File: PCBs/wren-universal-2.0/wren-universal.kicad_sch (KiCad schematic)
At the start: 121 parts, among them J1 TRRS_Jack, J2 Nice!Nano Compatibility, SW0 Reset, U1 Elite-C, U2 EGG PRO MICRO

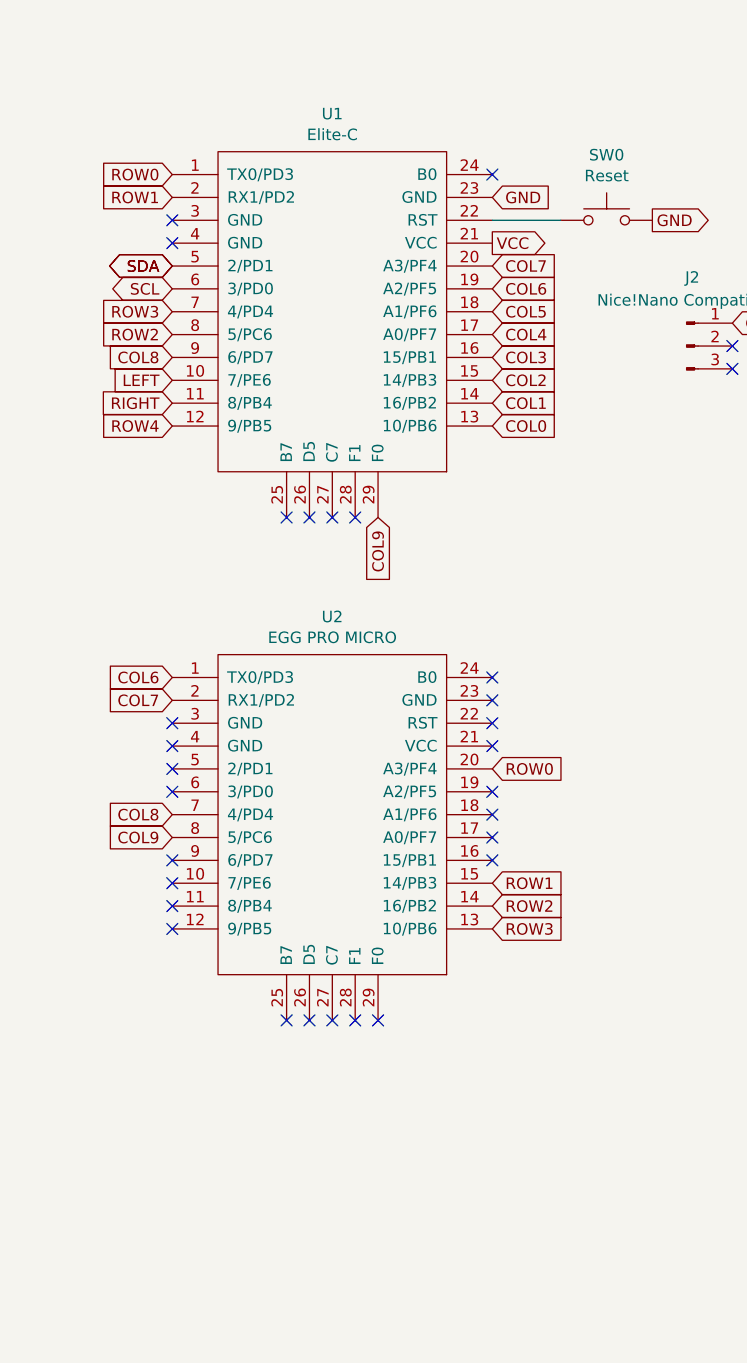
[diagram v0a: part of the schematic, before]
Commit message: Add battery header, update readme
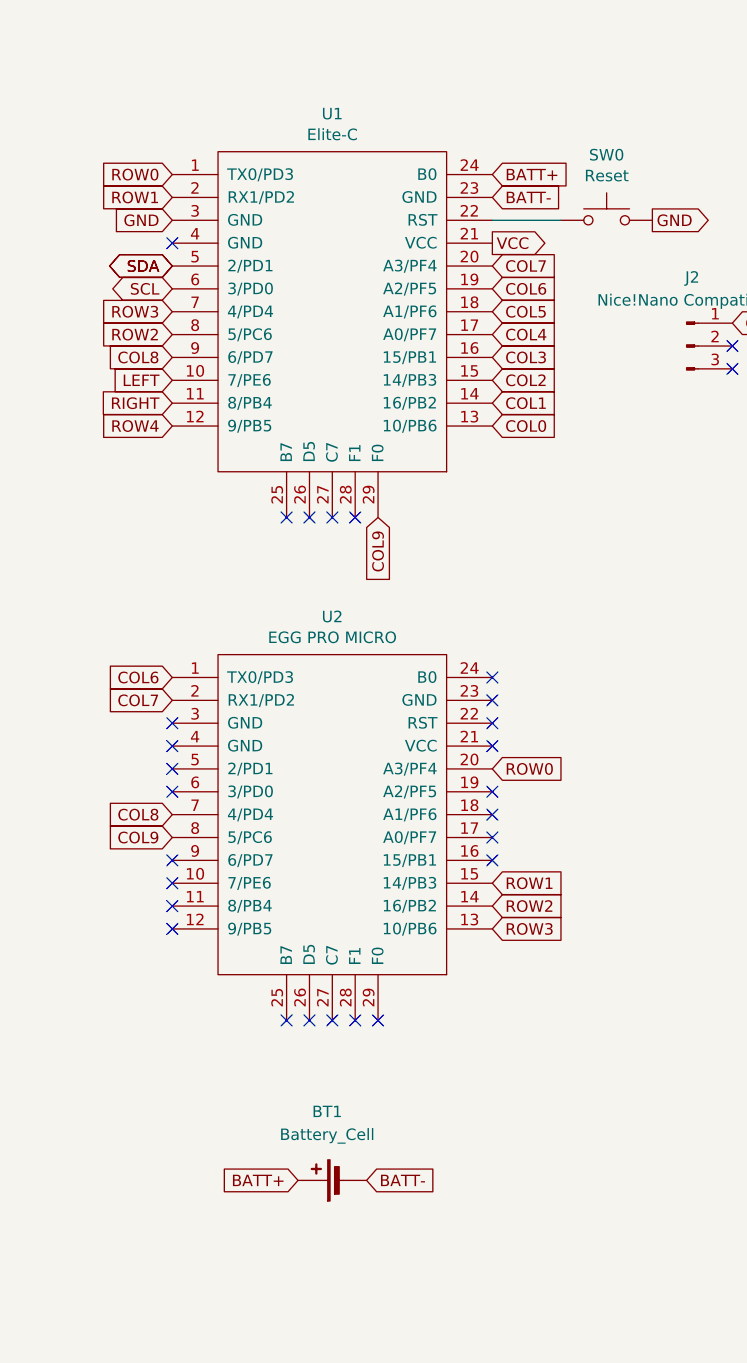
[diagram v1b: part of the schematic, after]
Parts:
- added BT1: Battery_Cell, Connector_PinHeader_2.00mm:PinHeader_1x02_P2.00mm_Vertical, symbol Device:Battery_Cell
- J2: footprint Connector_PinHeader_1.00mm:PinHeader_1x03_P1.00mm_Horizontal -> Connector_PinHeader_2.54mm:PinHeader_1x03_P2.54mm_Vertical
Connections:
- net GND: now also U1.3 (GND); no longer U1.23 (GND)
- net BATT+: now reaches U1.24 (B0)
- net BATT+: now also BT1.1 (+)
- new net BATT-: BT1.2 (-), U1.23 (GND)
- no-connect marks 30 -> 28
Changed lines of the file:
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@@
   (no_connect (at 44.45 118.11))
   (no_connect (at 80.01 105.41))
-  (no_connect (at 80.01 34.29))
   (no_connect (at 80.01 102.87))
   (no_connect (at 44.45 115.57))
@@
   (no_connect (at 57.15 128.27))
   (no_connect (at 62.23 72.39))
-  (no_connect (at 44.45 39.37))
   (wire (pts (xy 177.8 68.58) (xy 177.8 86.36))
     (stroke (width 0) (type default))
@@
     )
   )
+  (global_label "BATT-" (shape input) (at 80.01 36.83 0) (fields_autoplaced)
+    (effects (font (size 1.27 1.27)) (justify left))
+    (property "Intersheetrefs" "${INTERSHEET_REFS}" (at 88.2072 36.83 0)
+      (effects (font (size 1.27 1.27)) (justify left) hide)
+    )
+  )
   (global_label "COL5" (shape input) (at 80.01 49.53 0)
     (effects (font (size 1.27 1.27)) (justify left))
@@
     )
   )
+  (global_label "BATT+" (shape input) (at 80.01 34.29 0) (fields_autoplaced)
+    (effects (font (size 1.27 1.27)) (justify left))
+    (property "Intersheetrefs" "${INTERSHEET_REFS}" (at 88.2072 34.29 0)
+      (effects (font (size 1.27 1.27)) (justify left) hide)
+    )
+  )
   (global_label "COL5" (shape input) (at 228.6 24.13 90)
     (effects (font (size 1.27 1.27)) (justify left))
@@
     )
   )
-  (global_label "GND" (shape input) (at 80.01 36.83 0)
-    (effects (font (size 1.27 1.27)) (justify left))
-    (property "Intersheetrefs" "${INTERSHEET_REFS}" (at 80.01 36.83 0)
+  (global_label "BATT+" (shape input) (at 58.42 146.05 180) (fields_autoplaced)
+    (effects (font (size 1.27 1.27)) (justify right))
+    (property "Intersheetrefs" "${INTERSHEET_REFS}" (at 50.2228 146.05 0)
+      (effects (font (size 1.27 1.27)) (justify right) hide)
+    )
+  )
+  (global_label "GND" (shape input) (at 44.45 39.37 180)
+    (effects (font (size 1.27 1.27)) (justify right))
+    (property "Intersheetrefs" "${INTERSHEET_REFS}" (at 44.45 39.37 0)
       (effects (font (size 1.27 1.27)) hide)
     )
@@
     )
   )
+  (global_label "BATT-" (shape input) (at 66.04 146.05 0) (fields_autoplaced)
+    (effects (font (size 1.27 1.27)) (justify left))
+    (property "Intersheetrefs" "${INTERSHEET_REFS}" (at 74.2372 146.05 0)
+      (effects (font (size 1.27 1.27)) (justify left) hide)
+    )
+  )
   (global_label "COL6" (shape input) (at 241.3 24.13 90)
     (effects (font (size 1.27 1.27)) (justify left))
@@
       (effects (font (size 1.27 1.27)))
     )
-    (property "Footprint" "Connector_PinHeader_1.00mm:PinHeader_1x03_P1.00mm_Horizontal" (at 101.6 53.34 0)
+    (property "Footprint" "Connector_PinHeader_2.54mm:PinHeader_1x03_P2.54mm_Vertical" (at 101.6 53.34 0)
       (effects (font (size 1.27 1.27)) hide)
     )
@@
         )
       )
+    )
+  )
+  (symbol (lib_id "Device:Battery_Cell") (at 63.5 146.05 90) (unit 1)
+    (in_bom yes) (on_board yes) (dnp no) (fields_autoplaced)
+    (property "Reference" "BT1" (at 61.6585 138.43 90)
+      (effects (font (size 1.27 1.27)))
+    )
+    (property "Value" "Battery_Cell" (at 61.6585 140.97 90)
+      (effects (font (size 1.27 1.27)))
+    )
+    (property "Footprint" "Connector_PinHeader_2.00mm:PinHeader_1x02_P2.00mm_Vertical" (at 61.976 146.05 90)
+      (effects (font (size 1.27 1.27)) hide)
+    )
+    (property "Datasheet" "~" (at 61.976 146.05 90)
+      (effects (font (size 1.27 1.27)) hide)
+    )
+    (pin "1")
+    (pin "2")
+    (instances
+      (project "wren-universal"
+        (path "/ae419152-cad0-45f0-8aa2-3732c2e35dc1"
+          (reference "BT1") (unit 1)
+        )
+      )

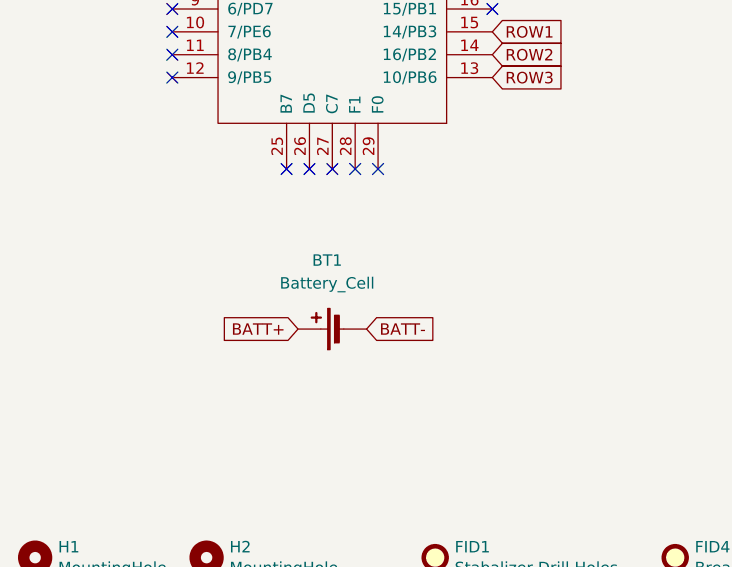
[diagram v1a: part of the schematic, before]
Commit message: Minor labeling changes
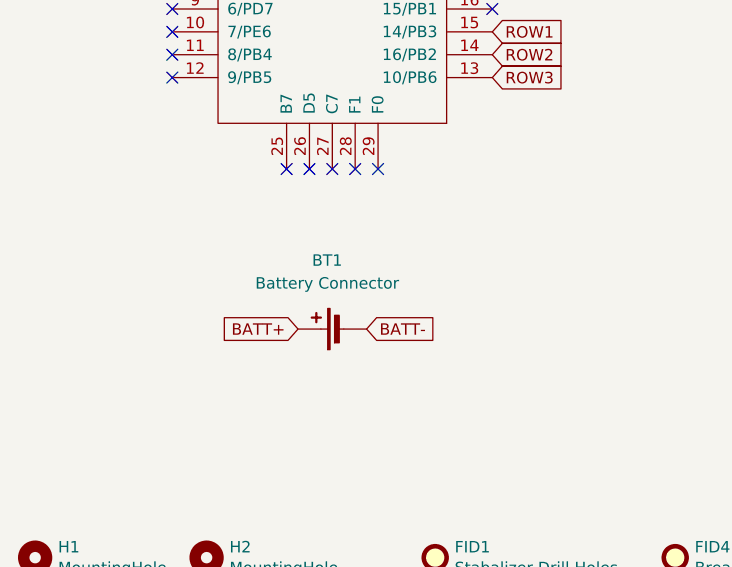
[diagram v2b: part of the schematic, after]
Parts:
- BT1: value Battery_Cell -> Battery Connector
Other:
- title: (none) -> Wren Keyboard PCB (Half)
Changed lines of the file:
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@@
 (kicad_sch (version 20230121) (generator eeschema)
   (paper "A4")
+  (title_block
+    (title "Wren Keyboard PCB (Half)")
+    (date "2024-10-23")
+    (rev "2.0")
+  )
   (junction (at 215.9 68.58) (diameter 0) (color 0 0 0 0)
   )
@@
       (effects (font (size 1.27 1.27)))
     )
-    (property "Value" "Battery_Cell" (at 61.6585 140.97 90)
+    (property "Value" "Battery Connector" (at 61.6585 140.97 90)
       (effects (font (size 1.27 1.27)))
     )
